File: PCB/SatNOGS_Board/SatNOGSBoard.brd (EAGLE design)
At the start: 59.4 x 68.6 mm, 17 parts, among them J1 2, J2 3, J3 4

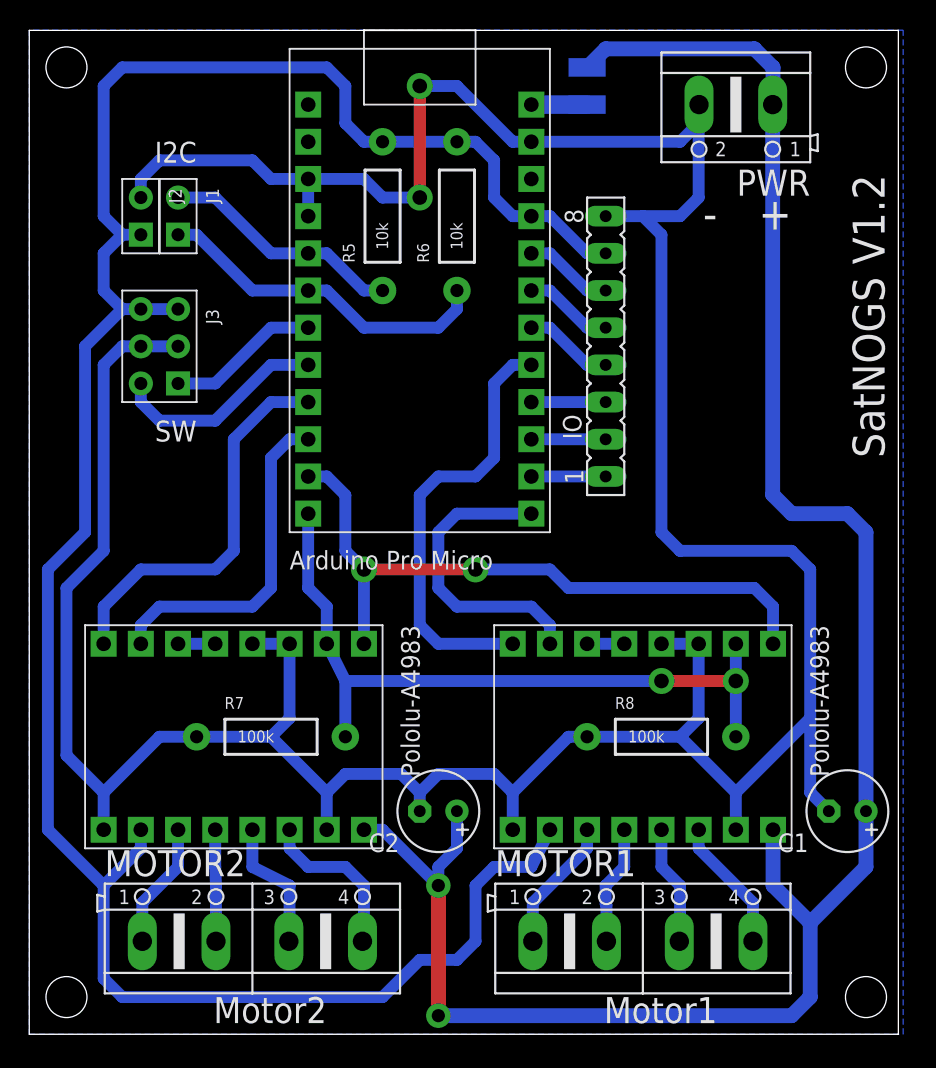
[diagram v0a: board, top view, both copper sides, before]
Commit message: schematic update, raw routing prototype
this adds the AtMega168 and neccesary components. Layout is just a raw
sketch, someone should finish that.
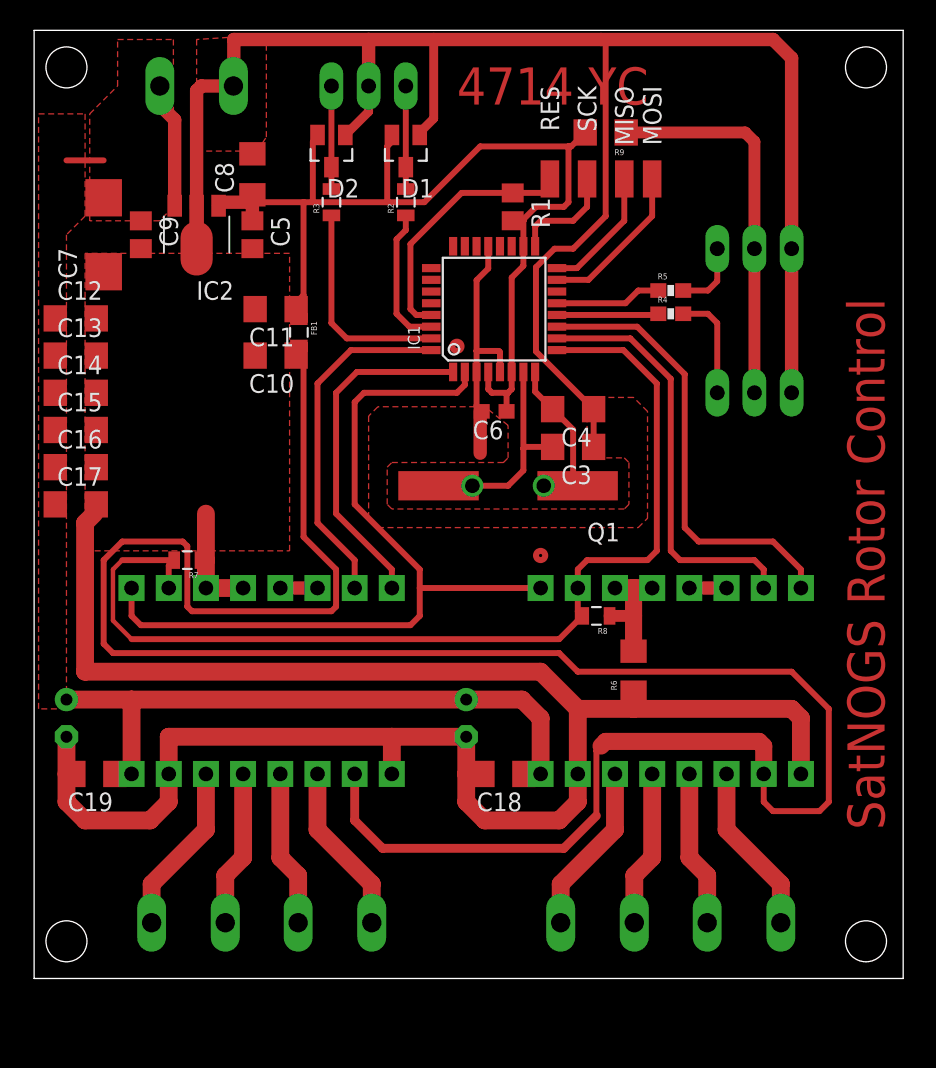
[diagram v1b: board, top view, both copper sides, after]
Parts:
- removed IO: 1, con-lsta:FE08
- removed J1: 2, Connector:2P-2.54-65/35MIL
- removed J2: 3, Connector:2P-2.54-65/35MIL
- removed J3: 4, Connector:2X3P-2.54-65/35MIL
- removed SJ1: SJ1, jumper:SJW
- removed UC: ARDUINO_PRO_MICROARDUINO_BOARD, Arduino_Pro_Micro:ARDUINO_MICRO_PRO
- added C10, C11, C12, C13, C14, C15, C16, C17, C18, C19, C8: 680n, rcl:C1206
- added C3, C4: 18p, rcl:C1206
- added C5, C9: 100n, rcl:C0805
- added C6: 100n, rcl:C0603
- added C7: (no value), rcl:C/6032-28R
- added D1, D2: BAV99, diode:SOT23
- added FB1: 10R@100MHz, SparkFun-Resistors:0805
- added IC1: MEGA8-AI, atmel:TQFP32-08
- added IC2: 78L05F, linear:SOT89
- added JP1, JP2, JP3: (no value), pinhead:1X03
- added MISO, MOSI, RES, SCK: (no value), wirepad:SMD1,27-2,54
- added Q1: 16MHz, crystal:CSM-7X-DU
- added R1: 4k7, rcl:R0805
- added R2: 1k, SparkFun-Resistors:0805
- added R3: 475R, SparkFun-Resistors:0805
- added R4: (no value), SparkFun-Resistors:0603-RES
- added R9: 0R, SparkFun-Resistors:1206
- R5: value 10k -> (none); device SparkFun-Resistors:AXIAL-0.4 -> SparkFun-Resistors:0603-RES
- R6: value 10k -> 0R; device SparkFun-Resistors:AXIAL-0.4 -> SparkFun-Resistors:1206
- R7, R8: device SparkFun-Resistors:AXIAL-0.4 -> SparkFun-Resistors:0805
- moved C1 53.7 mm to (2.54, 21.6), flipped to the bottom, turned to 270 degrees
- moved PWR 36.9 mm to (11.4, 64.8), flipped to the bottom
- moved R6 33.4 mm to (41.3, 24.8)
- moved DRIVER2 30.1 mm to (43.8, 24.1), flipped to the bottom
- moved MOTOR2 28.6 mm to (43.8, 7.62), flipped to the bottom
- moved DRIVER1 26.3 mm to (15.9, 24.1), flipped to the bottom
- moved MOTOR1 26.1 mm to (15.9, 7.62), flipped to the bottom
- moved R5 20.3 mm to (43.8, 50.8), turned to 0 degrees
- moved R7 13.4 mm to (10.8, 32.4), turned to 180 degrees
- moved R8 9.38 mm to (38.7, 28.6), turned to 180 degrees
- moved C2 6.63 mm to (29.8, 21.6), flipped to the bottom, turned to 270 degrees
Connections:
- removed net IO1: IO.6, UC.20
- removed net IO2: IO.5, UC.19
- removed net IO3: IO.4, UC.18
- removed net IO4: IO.3, UC.16
- removed net IO5: IO.2, UC.15
- removed net IO6: IO.1, UC.14
- removed net SCL: J1.1, R6.P$1, UC.6
- removed net SDA: J1.2, R5.P$1, UC.5
- removed net VCC: DRIVER1.10, DRIVER2.10, IO.7, J2.1, J3.3, J3.4, R5.P$2, R6.P$2, UC.21
- removed net VMOTOR: C1.+, C2.+, DRIVER1.16, DRIVER2.16, PWR.1, SJ1.2
- new net +12V: C1.+, C12.1, C13.1, C14.1, C15.1, C16.1, C17.1, C18.1, C19.1, C2.+, C7.+, C9.1, DRIVER1.16, DRIVER2.16, IC2.3, PWR.1
- new net +5V: C11.1, C5.1, C6.1, C8.1, D1.2, D2.2, FB1.1, IC1.18, IC1.4, IC1.6, IC2.1, R1.2, R9.2
- new net +5VM: C10.1, DRIVER1.10, DRIVER2.10, FB1.2
- new net N$10: IC1.16, MISO.1
- new net N$11: IC1.17, SCK.1
- new net N$12: IC1.12, R4.1
- new net N$13: DRIVER2.3, DRIVER2.4, R6.2, R8.1
- new net N$14: JP2.2, JP3.2, R9.1
- new net N$4: D2.3, JP1.3, R3.2
- new net N$5: IC1.29, R1.1, RES.1
- new net N$6: IC1.30, R2.1
- new net N$7: IC1.31, R3.1
- new net N$8: IC1.13, R5.1
- new net N$9: IC1.15, MOSI.1
- new net XTAL1: C3.2, IC1.7, Q1.2
- new net XTAL2: C4.2, IC1.8, Q1.1
- net DIR-1: now also IC1.1; no longer UC.17
- net DIR-2: now also IC1.11; no longer UC.9
- net GND: now also C10.2, C11.2, C12.2, C13.2, C14.2, C15.2, C16.2, C17.2, C18.2, C19.2, C3.1, C4.1, C5.2, C6.2, C7.-, C8.2, C9.2, D1.1, D2.1, IC1.21, IC1.3, IC1.5, IC2.2, IC2.2@1, JP1.2, JP2.3, JP3.3, R6.1, R7.1; no longer DRIVER2.3, DRIVER2.4, IO.8, J2.2, J3.2, J3.5, R7.P$1, R8.P$1, UC.23, UC.3, UC.4
- net MS1: now also IC1.9, R7.2, R8.2; no longer R7.P$2, R8.P$2, UC.12
- net M_EN: now also IC1.2; no longer UC.11
- net N$3: now also D1.3, JP1.1, R2.2; no longer SJ1.1, UC.24
- net STEP-1: now also IC1.32; no longer UC.13
- net STEP-2: now also IC1.10; no longer UC.10
- net SW1: now also JP2.1, R5.2; no longer J3.1, UC.7
- net SW2: now also JP3.1, R4.2; no longer J3.6, UC.8
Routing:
- net VCC: track 157.7 -> 0.00 mm
- net +5VM: track 0.00 -> 150.3 mm
- net VMOTOR: track 138.2 -> 0.00 mm, vias 2 -> 0
- net +5V: track 0.00 -> 71.2 mm
- net +12V: track 0.00 -> 55.2 mm
- net GND: track 242.8 -> 278.9 mm, vias 2 -> 0
- net N$14: track 0.00 -> 26.2 mm
- net SCL: track 23.5 -> 0.00 mm
- net MS1: track 49.1 -> 71.9 mm, vias 2 -> 0
- net N$5: track 0.00 -> 17.8 mm
- net SDA: track 16.6 -> 0.00 mm
- net XTAL1: track 0.00 -> 15.0 mm, vias 0 -> 1
- net N$7: track 0.00 -> 14.6 mm
- net XTAL2: track 0.00 -> 11.5 mm, vias 0 -> 1
- net N$9: track 0.00 -> 10.8 mm
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- added copper zone on layer 1, net +12V
- added copper zone on layer 1, net GND
- removed copper zone on layer 16, net GND
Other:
- board size 59.4 x 68.6 mm -> 59.4 x 64.8 mm
- board text added: "4714 YC"
- board text added: "SatNOGS Rotor Control"
- board text removed: "+"
- board text removed: "-"
- board text removed: "I2C"
- board text removed: "Motor1"
- board text removed: "Motor2"
- board text removed: "SW"
- board text removed: "SatNOGS V1.2"
